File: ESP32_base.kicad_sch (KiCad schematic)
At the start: 32 parts, among them J1 Conn_01x16_Socket, J2 Conn_01x16_Socket, J3 Conn_01x04_Socket, J5 KH-IPEXA-SMAKWE-B080H, SW1 boot, SW2 reset, U1 ADT7310TRZ, U2 3.3V, U3 ESP32-C5-WROOM-1U-N8-R4

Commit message: remove BOM spam
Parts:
- FB1: Mfr. part (none) -> MPZ2012S601AT000; Mrf part MPZ2012S601AT000 -> (none)
- FB2: Mfr. Part (none) -> SRP3212A-4R7M; Part SRP3212A-4R7M -> (none)
- J3: Mfr. Part (none) -> 2.54-1*4P; Mrf. Part 2.54-1*4P -> (none)
- J5: footprint Connector_Coaxial:SMA_Amphenol_132203-12_Horizontal -> easyeda2kicad:CONN-TH_KH-IPEX-SMAKWE; Mfr. Part (none) -> KH-IPEXA-SMAKWE-B080H
- SW1, SW2: Mfr. Part (none) -> TS-1002S-04526C

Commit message: wip
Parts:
- AE1: Mrf. Part HJ-2.4G/5G-PCB-SMA-RG141-L47mm -> (none)
- C2: Mrf CC0805KRX7R9BB104 -> (none)
- FB1: Mfr. part MPZ2012S601AT000 -> (none)

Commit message: BOM spam
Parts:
- C1: LCSC C83170 -> (none); LCSC Part (none) -> C83170; Mfr. Part (none) -> CC0805KRX7R9BB103; Part CC0805KRX7R9BB103 -> (none)
- C12, C9: LCSC C28323 -> (none); LCSC Part (none) -> C28323; Mfr. Part (none) -> CL21B105KBFNNNE; Part CL21B105KBFNNNE -> (none)
- C13, C4: LCSC C440198 -> (none); LCSC Part (none) -> C440198; Mfr. Part (none) -> GRM21BR61H106KE43L; Part GRM21BR61H106KE43L -> (none)
- C2: LCSC C49678 -> (none); LCSC Part (none) -> C49678; Mfr. Part (none) -> CC0805KRX7R9BB104
- C3: Mfr. Part (none) -> GRM21BZ71H475KE15L; Part GRM21BZ71H475KE15L -> (none)
- C5, C8: LCSC C49678 -> (none); LCSC Part (none) -> C49678; Mfr. Part (none) -> CC0805KRX7R9BB104; Part CC0805KRX7R9BB104 -> (none)
- C6, C7: LCSC C6119901 -> (none); LCSC Part (none) -> C6119901; Mfr. Part (none) -> CGA0805X5R226M350MT; Part CGA0805X5R226M350MT -> (none)
- FB2: LCSC C19190305 -> (none); LCSC Part (none) -> C19190305
- R3, R5: LCSC C84376 -> (none); LCSC Part (none) -> C84376; Mfr. Part (none) -> RC0805FR-0710KL; Part RC0805FR-0710KL -> (none)
- R4: LCSC C17520 -> (none); LCSC Part (none) -> C17520; Mfr. Part (none) -> 0805W8F2201T5E; Part 0805W8F2201T5E -> (none)
- R7:  LCSC Part (none) -> C84376; LCSC C84376 -> (none); Mfr. Part (none) -> RC0805FR-0710KL; Part RC0805FR-0710KL -> (none)

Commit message: remove BOM spam
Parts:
- FB1: Mfr. Part (none) -> MPZ2012S601AT000
- R7:  LCSC Part C84376 -> (none); LCSC Part (none) -> C84376
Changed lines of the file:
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@@
 			)
 		)
-		(property " LCSC Part" "C84376"
+		(property "LCSC Part" "C84376"
 			(at 41.91 275.59 90)
 			(effects
@@
 			(effects
 				(font
+					(size 1.27 1.27)
+				)
+				(hide yes)
+			)
+		)
+		(property "Mfr. Part" "MPZ2012S601AT000"
+			(at 116.84 133.35 90)
+			(effects
+				(font

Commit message: remove BOM spam
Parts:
- C3: LCSC C437557 -> (none); LCSC Part (none) -> C437557
- LED1: LCSC C84260 -> (none); LCSC Part (none) -> C84260; Mfr. Part (none) -> NCD0805G1; Part NCD0805G1 -> (none)
- R1, R2: LCSC C27834 -> (none); LCSC Part (none) -> C27834; Mfr. Part (none) -> 0805W8F5101T5E; Part 0805W8F5101T5E -> (none)
- U2: LCSC C780769 -> (none); LCSC Part (none) -> C780769
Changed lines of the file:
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@@
 			)
 		)
-		(property "LCSC" "C27834"
+		(property "LCSC Part" "C27834"
 			(at 60.96 111.76 0)
 			(effects
@@
 			)
 		)
-		(property "Part" "0805W8F5101T5E"
+		(property "Mfr. Part" "0805W8F5101T5E"
 			(at 60.96 111.76 0)
 			(effects
@@
 			)
 		)
-		(property "LCSC" "C27834"
+		(property "LCSC Part" "C27834"
 			(at 60.96 116.84 0)
 			(effects
@@
 			)
 		)
-		(property "Part" "0805W8F5101T5E"
+		(property "Mfr. Part" "0805W8F5101T5E"
 			(at 60.96 116.84 0)
 			(effects
@@
 			)
 		)
-		(property "LCSC" "C84260"
+		(property "LCSC Part" "C84260"
 			(at 151.13 306.07 0)
 			(effects
@@
 			)
 		)
-		(property "Part" "NCD0805G1"
+		(property "Mfr. Part" "NCD0805G1"
 			(at 151.13 306.07 0)
 			(effects
@@
 			)
 		)
-		(property "LCSC" "C780769"
+		(property "LCSC Part" "C780769"
 			(at 67.31 181.61 0)
 			(effects
@@
 			)
 		)
-		(property "LCSC" "C437557"
+		(property "LCSC Part" "C437557"
 			(at 139.7 137.16 0)
 			(effects

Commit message: production_13_01_26
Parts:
- FB2: LCSC Part C19190305 -> (none)
- J1, J2: LCSC Part C2905421 -> C19190305

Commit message: BOM: fix 01x16 connector
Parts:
- J2: LCSC Part C19190305 -> C2905421
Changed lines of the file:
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@@
 			)
 		)
-		(property "LCSC Part" "C19190305"
+		(property "LCSC Part" "C2905421"
 			(at 234.95 106.68 0)
 			(effects
@@
 			(at 234.95 106.68 0)
 			(effects
-				(font
-					(size 1.27 1.27)
-				)
-				(hide yes)
-			)
-		)
-		(property "LCSC" ""
-			(at 234.95 106.68 0)
-			(effects
-				(font
-					(size 1.27 1.27)
-				)
-				(hide yes)
-			)
-		)
-		(property "Part" ""
-			(at 234.95 106.68 0)
-			(effects

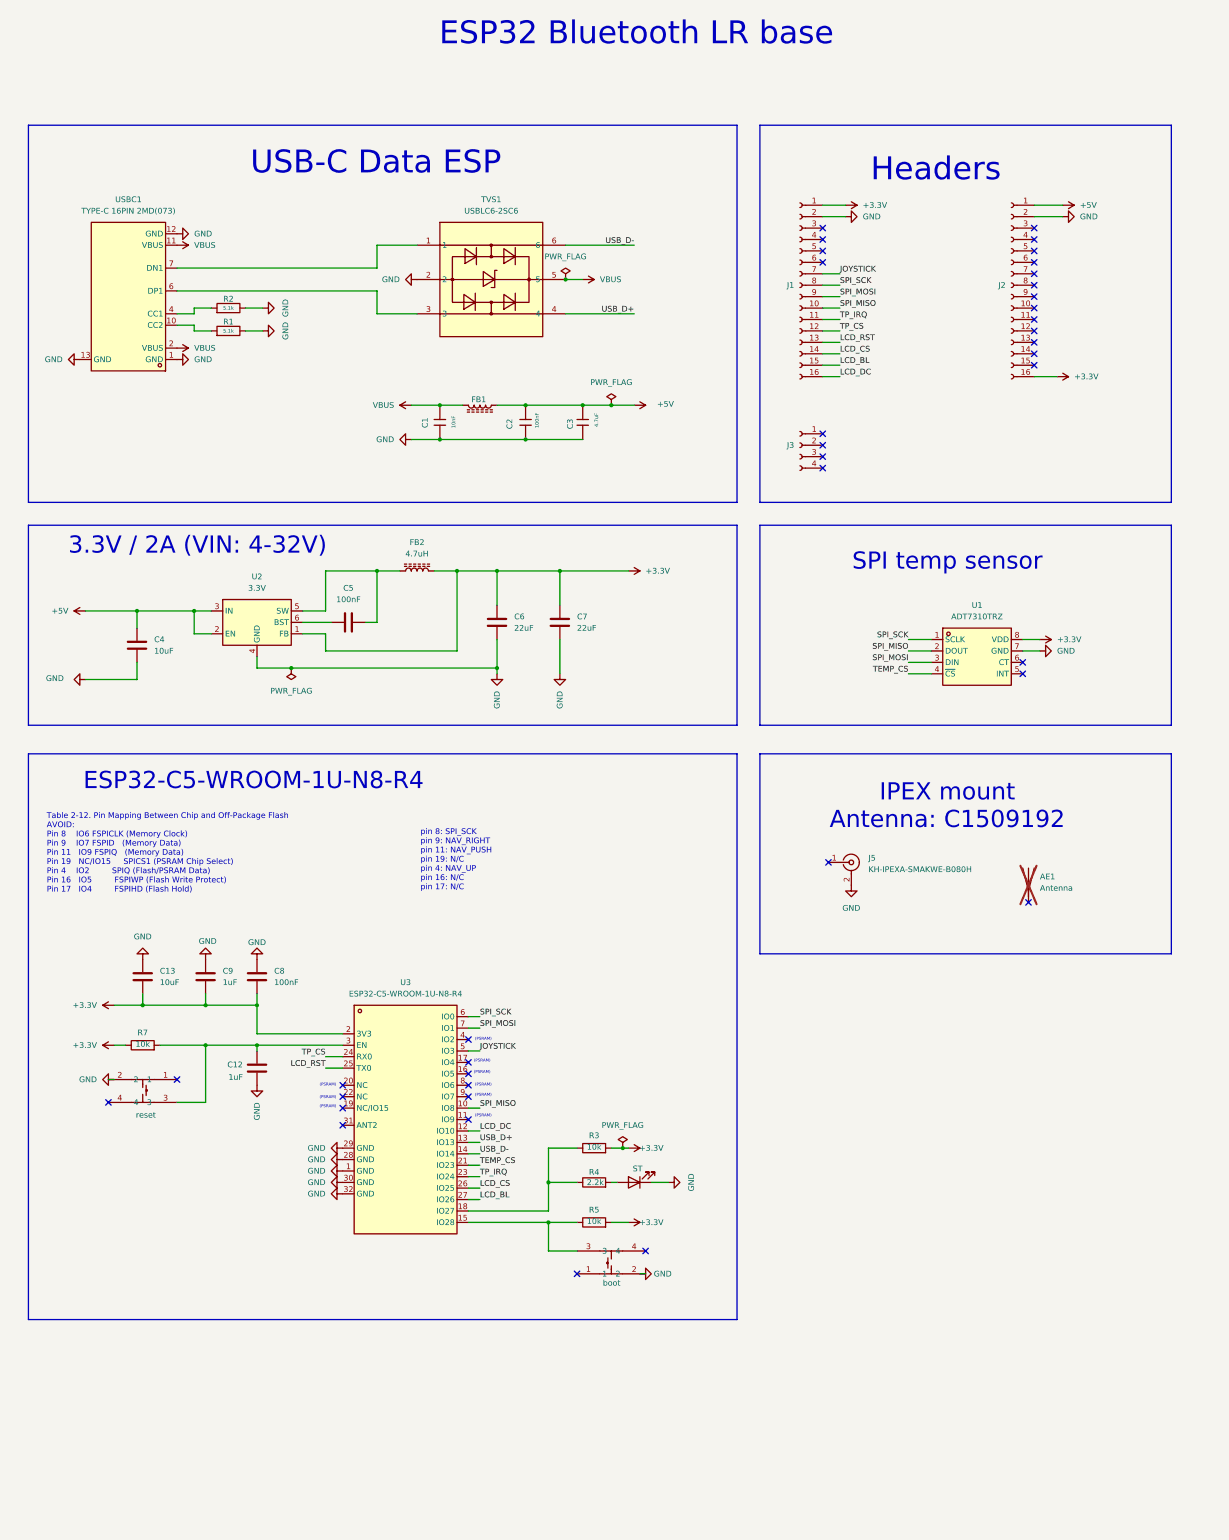
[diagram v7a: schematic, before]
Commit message: MCP: re-route and reallocate pins. Additionally, define ADC pins
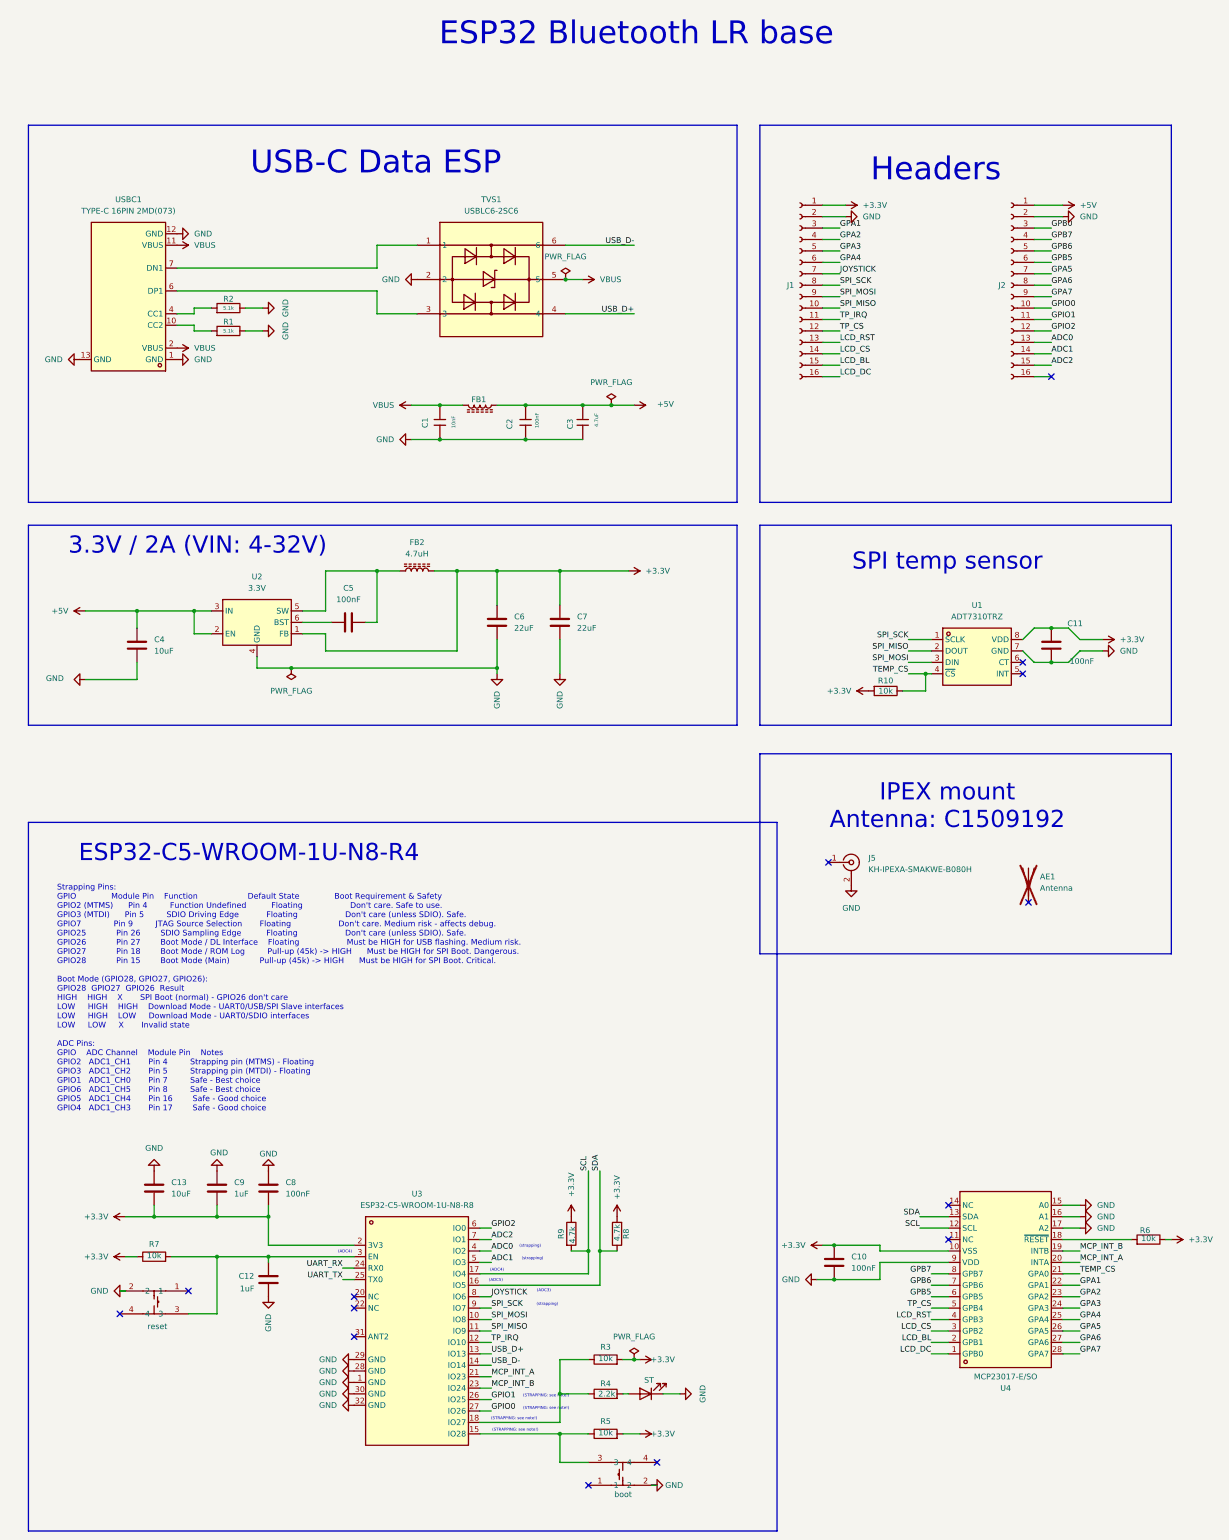
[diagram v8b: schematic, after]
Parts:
- removed J3: Conn_01x04_Socket, Connector_PinSocket_2.54mm:PinSocket_1x04_P2.54mm_Vertical, symbol Connector:Conn_01x04_Socket
- added C10, C11: 100nF, Capacitor_SMD:C_0805_2012Metric, symbol Device:C
- added R10, R6: 10k, Resistor_SMD:R_0805_2012Metric, symbol Device:R
- added R8, R9: 4.7k, Resistor_SMD:R_0805_2012Metric, symbol Device:R
- added U4: MCP23017-E/SO, easyeda2kicad:SOIC-28_L18.0-W7.5-P1.27-LS10.3-BL, symbol easyeda2kicad:MCP23017-E_SO
- R3, R4, R5, R7: footprint PCM_JLCPCB:R_0805 -> Resistor_SMD:R_0805_2012Metric
- U3: value ESP32-C5-WROOM-1U-N8-R4 -> ESP32-C5-WROOM-1U-N8-R8
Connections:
- net +3.3V: now also C10.1, C11.1, R10.2, R6.1, R8.2, R9.1, U4.10 (VSS); no longer J2.16 (Pin_16)
- net GND: now also C10.2, C11.2, U4.15 (A0), U4.16 (A1), U4.17 (A2), U4.9 (VDD)
- net JOYSTICK: now also U3.8 (IO6); no longer U3.5 (IO3)
- net LCD_BL: now also U4.2 (GPB1); no longer U3.27 (IO26)
- net LCD_CS: now also U4.3 (GPB2); no longer U3.26 (IO25)
- net LCD_DC: now also U4.1 (GPB0); no longer U3.12 (IO10)
- net LCD_RST: now also U4.4 (GPB3); no longer U3.25 (TX0)
- net SPI_MISO: now also U3.11 (IO9); no longer U3.10 (IO8)
- net SPI_MOSI: now also U3.10 (IO8); no longer U3.7 (IO1)
- net SPI_SCK: now also U3.9 (IO7); no longer U3.6 (IO0)
- net TEMP_CS: now also R10.1, U4.21 (GPA0); no longer U3.21 (IO23)
- net TP_CS: now also U4.5 (GPB4); no longer U3.24 (RX0)
- net TP_IRQ: now also U3.12 (IO10); no longer U3.23 (IO24)
- net SDA: now reaches U3.16 (IO5)
- net SDA: now also R8.1, U4.13 (SDA)
- net SCL: now reaches U3.17 (IO4)
- net SCL: now also R9.2, U4.12 (SCL)
- net ADC0: now reaches U3.4 (IO2)
- net ADC0: now also J2.13 (Pin_13)
- net GPIO0: now reaches J2.10 (Pin_10)
- net GPIO0: now also U3.27 (IO26)
- net GPIO1: now reaches J2.11 (Pin_11)
- net GPIO1: now also U3.26 (IO25)
- net GPIO2: now reaches J2.12 (Pin_12)
- net GPIO2: now also U3.6 (IO0)
- net ADC1: now reaches J2.14 (Pin_14)
- net ADC1: now also U3.5 (IO3)
- net ADC2: now reaches J2.15 (Pin_15)
- net ADC2: now also U3.7 (IO1)
- net GPB0: now reaches J2.3 (Pin_3)
- net GPB7: now reaches J2.4 (Pin_4)
- net GPB7: now also U4.8 (GPB7)
- net GPB6: now reaches J2.5 (Pin_5)
- net GPB6: now also U4.7 (GPB6)
- net GPB5: now reaches J2.6 (Pin_6)
- net GPB5: now also U4.6 (GPB5)
- net GPA5: now reaches J2.7 (Pin_7)
- net GPA5: now also U4.26 (GPA5)
- net GPA6: now reaches J2.8 (Pin_8)
- net GPA6: now also U4.27 (GPA6)
- net GPA7: now reaches J2.9 (Pin_9)
- net GPA7: now also U4.28 (GPA7)
- net GPA1: now reaches J1.3 (Pin_3)
- net GPA1: now also U4.22 (GPA1)
- net GPA2: now reaches J1.4 (Pin_4)
- net GPA2: now also U4.23 (GPA2)
- net GPA3: now reaches J1.5 (Pin_5)
- net GPA3: now also U4.24 (GPA3)
- net GPA4: now reaches J1.6 (Pin_6)
- net GPA4: now also U4.25 (GPA4)
- new net: R6.2, U4.18 (~{RESET})
- new net MCP_INT_A: U3.21 (IO23), U4.20 (INTA)
- new net MCP_INT_B: U3.23 (IO24), U4.19 (INTB)
- new net UART_RX: U3.24 (RX0)
- new net UART_TX: U3.25 (TX0)
- no-connect marks 39 -> 14
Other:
- note added: "(ADC3)"
- note added: "(ADC4)"
- note added: "(ADC5)"
- note added: "(STRAPPING: see note!)"
- note added: "(strapping)"
- note added: "Strapping Pins: GPIO Module Pin Function Default State Boot Requirement & Safety GPIO2 (MTMS) Pin 4 Function Undefined Floating Don't care. Safe to use. GPIO3 (MTDI) Pin 5 SDIO Driving Edge Floating Don't care (unless SDIO). Safe. GPIO7 Pin 9 JTAG Source Selection Floating Don't care. Medium risk - affects debug. GPIO25 Pin 26 SDIO Sampling Edge Floating Don't care (unless SDIO). Safe. GPIO26 Pin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"
- note removed: "(PSRAM)"
- note removed: "Table 2-12. Pin Mapping Between Chip and Off-Package Flash AVOID: Pin 8 IO6 FSPICLK (Memory Clock) Pin 9 IO7 FSPID (Memory Data) Pin 11 IO9 FSPIQ (Memory Data) Pin 19 NC/IO15 SPICS1 (PSRAM Chip Select) Pin 4 IO2 SPIQ (Flash/PSRAM Data) Pin 16 IO5 FSPIWP (Flash Write Protect) Pin 17 IO4 FSPIHD (Flash Hold)"
- note removed: "pin 8: SPI_SCK pin 9: NAV_RIGHT pin 11: NAV_PUSH pin 19: N/C pin 4: NAV_UP pin 16: N/C pin 17: N/C"
- moved on the sheet: C12, C13, C8, C9, R3, R4, R5, R7
